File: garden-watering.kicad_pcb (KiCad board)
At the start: 2 copper layers, 104.6 x 66.8 mm, 76 parts, among them J1 GND, J10 Screw_Terminal_01x02, J11 Screw_Terminal_01x02, J12 USB_C_Receptacle, J2 GND, J3 +3.3V, J4 +12V, J5 GPIO, J6 UART, J7 JTAG, J8 Screw_Terminal_01x02, J9 Screw_Terminal_01x02, K1 SANYOU_SRD_Form_C, K2 SANYOU_SRD_Form_C, K3 SANYOU_SRD_Form_C, K4 SANYOU_SRD_Form_C, Q1 2N2222, Q2 2N2222, Q3 2N2222, Q4 2N2222, SW1 RESET, SW2 PROG, SW3 SW_SPDT, SW4 SW_SPDT, SW5 SW_SPDT, SW6 SW_SPDT, U1 ESP32-WROOM-32, U2 DHT11, U3 LM1117T-3.3, U4 LM2576T-12

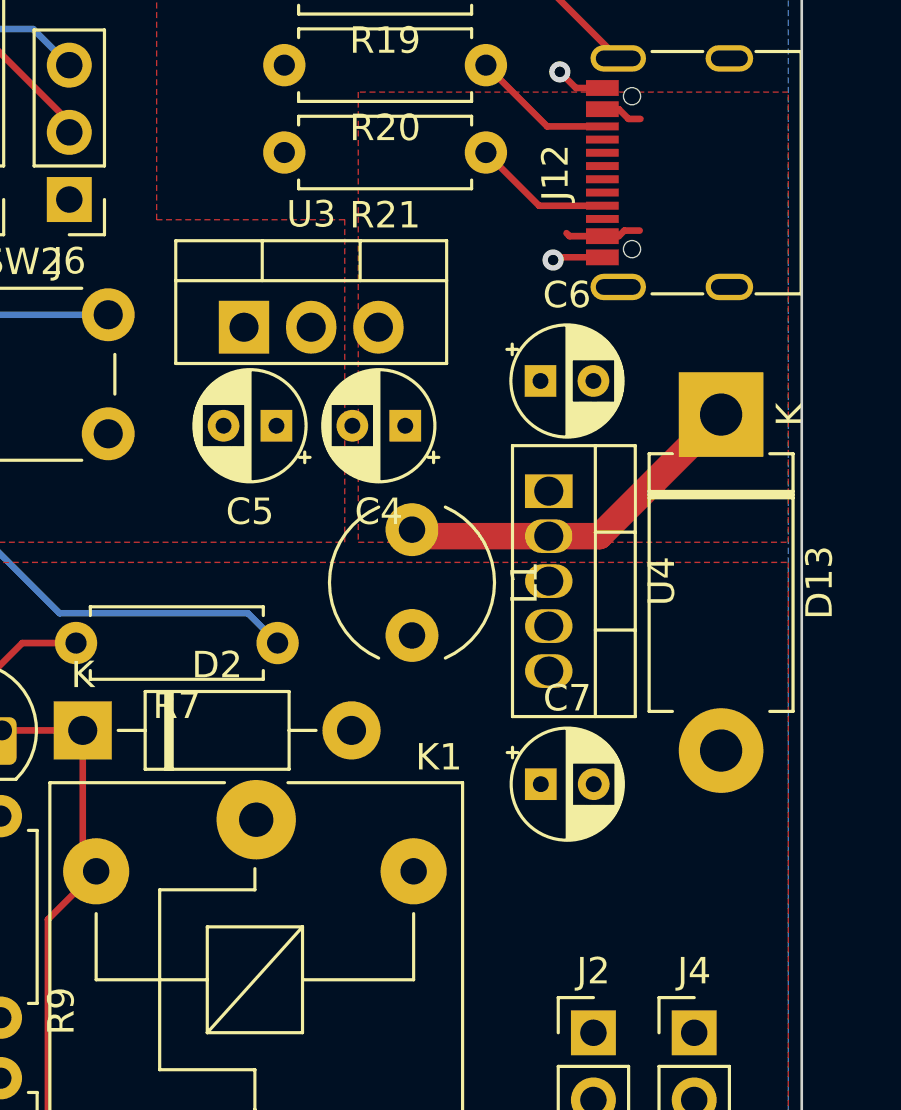
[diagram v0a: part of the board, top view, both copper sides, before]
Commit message: better footprint for hand soldering
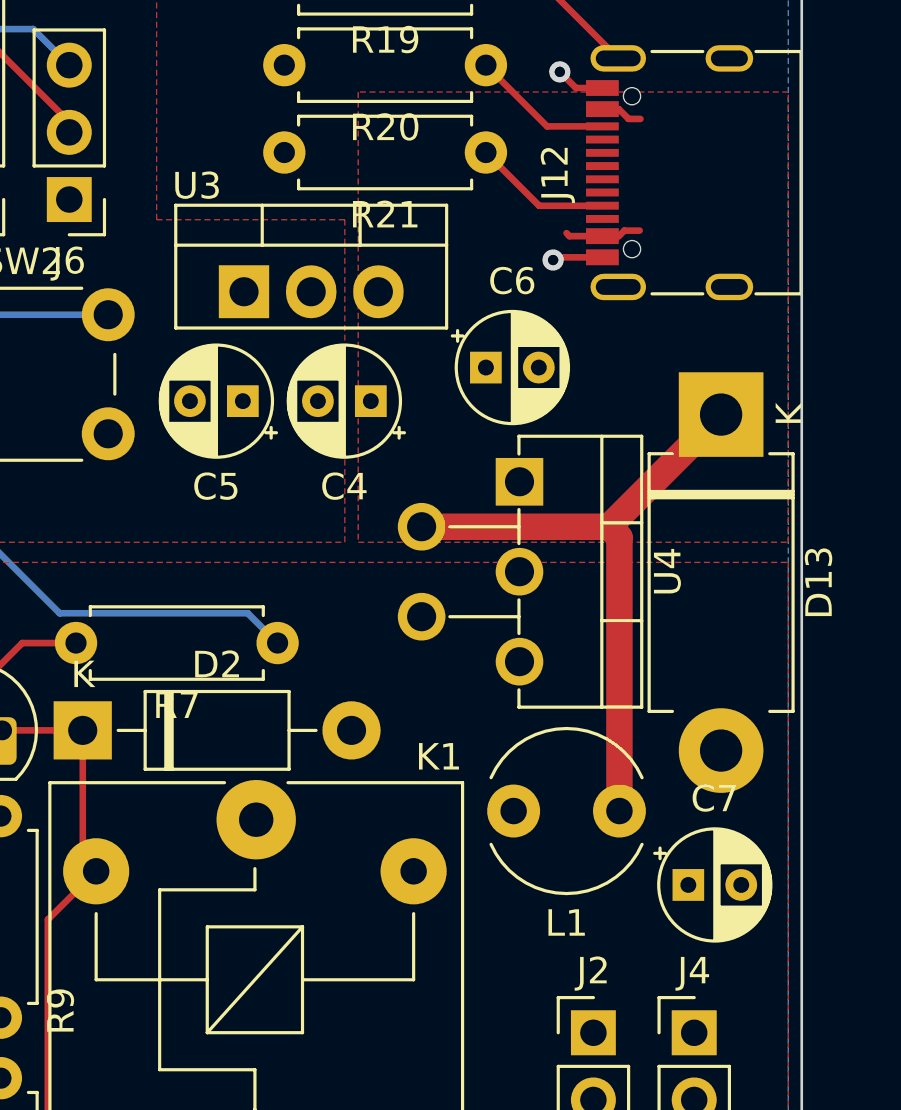
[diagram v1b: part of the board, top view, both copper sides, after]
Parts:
- U4: footprint Package_TO_SOT_THT:TO-220-5_Vertical -> Package_TO_SOT_THT:TO-220-5_P3.4x3.7mm_StaggerEven_Lead3.8mm_Vertical
- moved L1 13.2 mm to (196.6, 84.6), turned to 180 degrees
- moved C7 6.75 mm to (199.2, 87.4)
- moved C6 2.13 mm to (191.5, 67.8)
- moved C4 1.60 mm to (187.2, 69.1)
- moved C5 1.57 mm to (182.3, 69.1)
- moved U3 1.34 mm to (182.4, 65.0)
- moved U4 1.16 mm to (192.8, 72.1)
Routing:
- net Net-(D13-K): track 13.7 -> 24.3 mm
